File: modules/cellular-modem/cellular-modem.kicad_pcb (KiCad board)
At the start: 2 copper layers, 42.8 x 71.1 mm, 21 parts, among them J1 MM60-mini-PCIe, J2 MM60-EZH059-B5-R650, U1 TXV0108RGYR, U2 TXV0108RGYR, U3 TXV0108RGYR, U4 TPS631000DRLR, U5 TPS631000DRLR

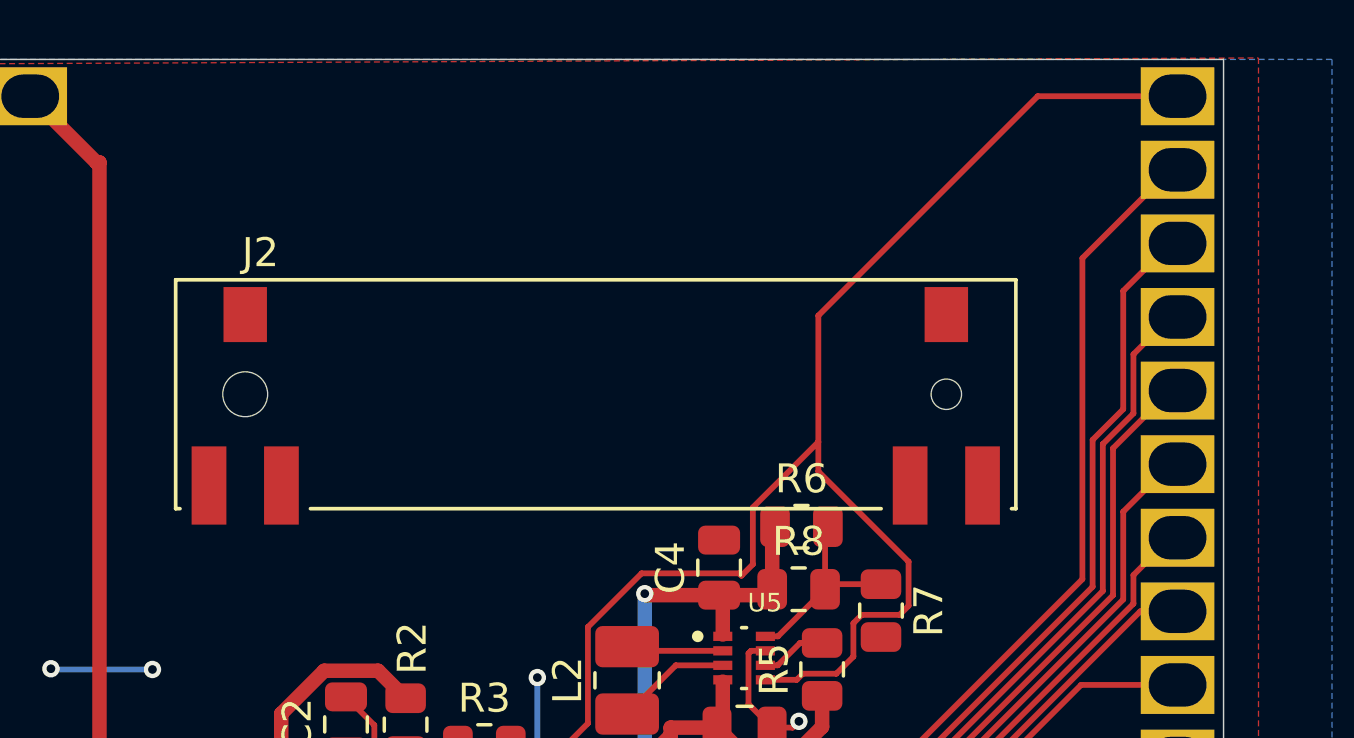
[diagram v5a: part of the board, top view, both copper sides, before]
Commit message: add missing shield pads to MM60 retainer
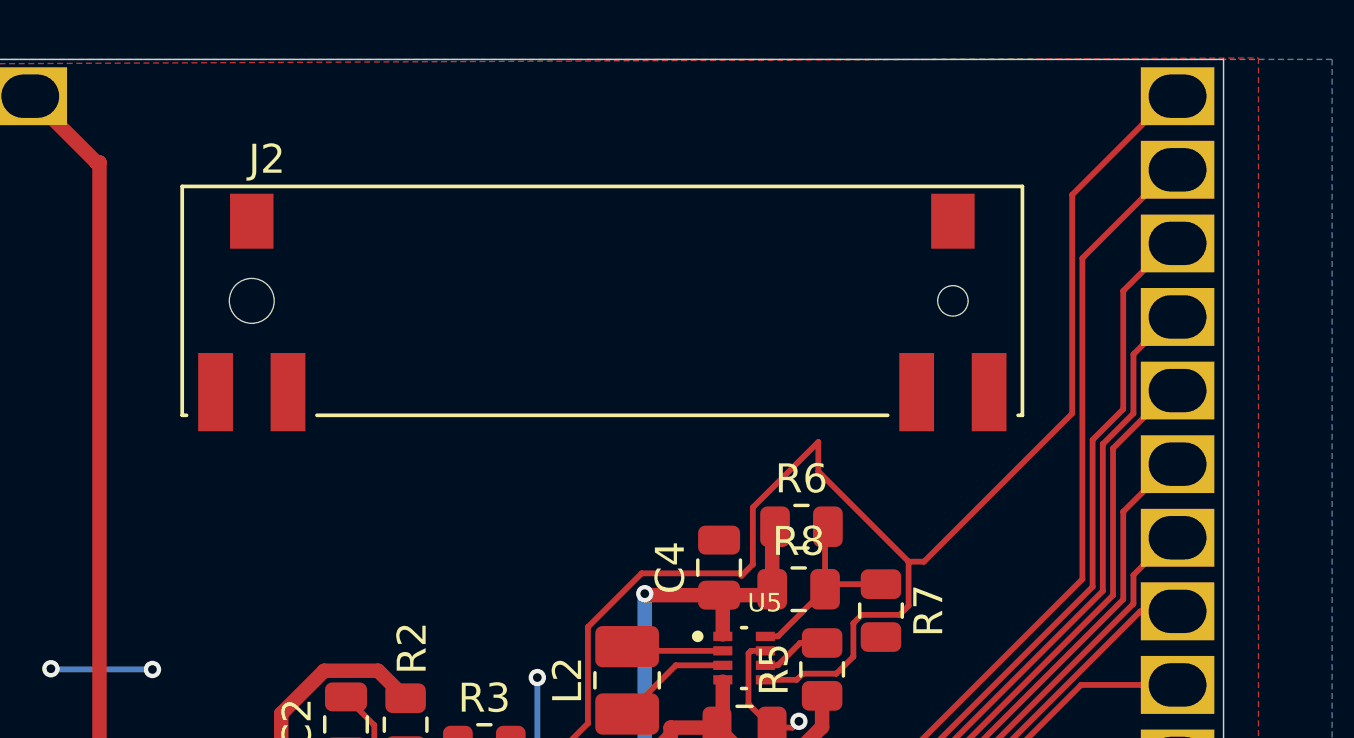
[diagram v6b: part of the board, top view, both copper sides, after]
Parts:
- moved J2 3.23 mm to (89.1, 43.9)
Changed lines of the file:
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@@
 	(footprint "cellular-modem:JAE_MM60-EZH059-B5-R650"
 		(layer "F.Cu")
-		(at 88.885 47.1166)
+		(at 89.1116 43.893799)
 		(property "Reference" "J2"
 			(at -11.575 -4.885 0)
@@
 	)
 	(segment
-		(start 108.966 36.83)
-		(end 104.14 36.83)
+		(start 99.3696 54.7322)
+		(end 98.064772 54.7322)
 		(width 0.2)
 		(layer "F.Cu")
@@
 	)
 	(segment
-		(start 99.3696 54.7322)
-		(end 98.064772 54.7322)
+		(start 100.2158 52.8954)
+		(end 99.6822 52.8954)
 		(width 0.2)
 		(layer "F.Cu")
@@
 	)
 	(segment
-		(start 97.7774 55.019572)
-		(end 97.7774 56.172)
+		(start 105.3292 40.232)
+		(end 105.3292 47.782)
 		(width 0.2)
 		(layer "F.Cu")
@@
 	)
 	(segment
-		(start 82.126369 62.41684)
-		(end 81.6902 62.41684)
+		(start 97.7774 55.019572)
+		(end 97.7774 56.172)
 		(width 0.2)
 		(layer "F.Cu")
@@
 	)
 	(segment
-		(start 96.567036 44.402964)
-		(end 96.567036 48.764236)
+		(start 82.126369 62.41684)
+		(end 81.6902 62.41684)
 		(width 0.2)
 		(layer "F.Cu")
@@
 	)
 	(segment
+		(start 105.3292 47.782)
+		(end 100.2158 52.8954)
+		(width 0.2)
+		(layer "F.Cu")
+		(net 78)
+	)
+	(segment
+		(start 108.966 36.83)
+		(end 108.7312 36.83)
+		(width 0.2)
+		(layer "F.Cu")
+		(net 78)
+	)
+	(segment
 		(start 96.032772 56.7623)
 		(end 95.821472 56.9736)
@@
 	)
 	(segment
+		(start 108.7312 36.83)
+		(end 105.3292 40.232)
+		(width 0.2)
+		(layer "F.Cu")
+		(net 78)
+	)
+	(segment
 		(start 96.567036 48.764236)
 		(end 94.3073 51.023972)
@@
 		(width 0.2)
 		(layer "F.Cu")
-		(net 78)
-	)
-	(segment
-		(start 104.14 36.83)
-		(end 96.567036 44.402964)
-		(width 0.2)
-		(layer "F.Cu")
